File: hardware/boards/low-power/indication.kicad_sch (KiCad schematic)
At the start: 14 parts, among them Q1 DMN2400UFB4, U5 IS31FL3197

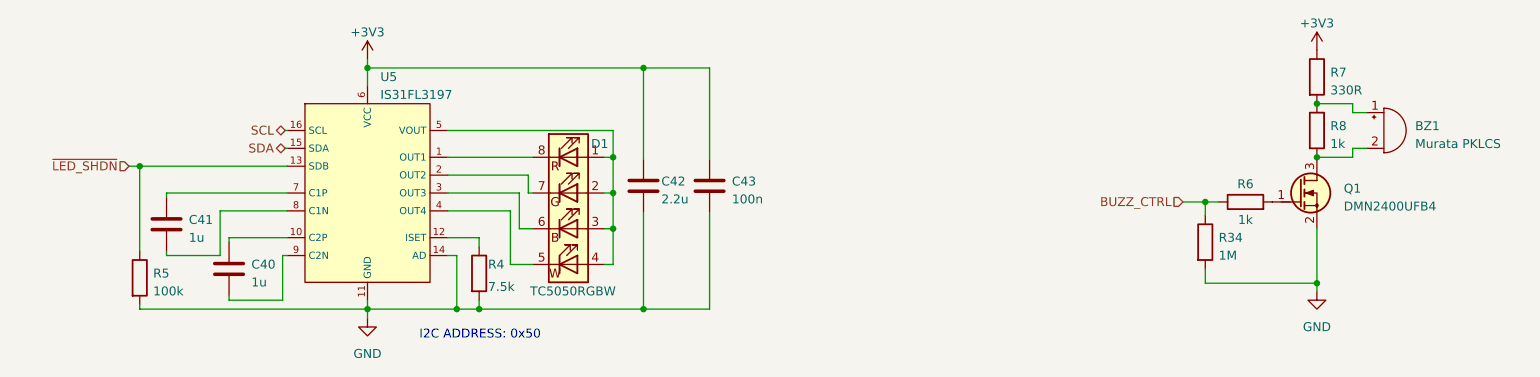
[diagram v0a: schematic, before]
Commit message: Add footprints and models for LP board
Also completed rough layout for LP board to estimate board space usage.
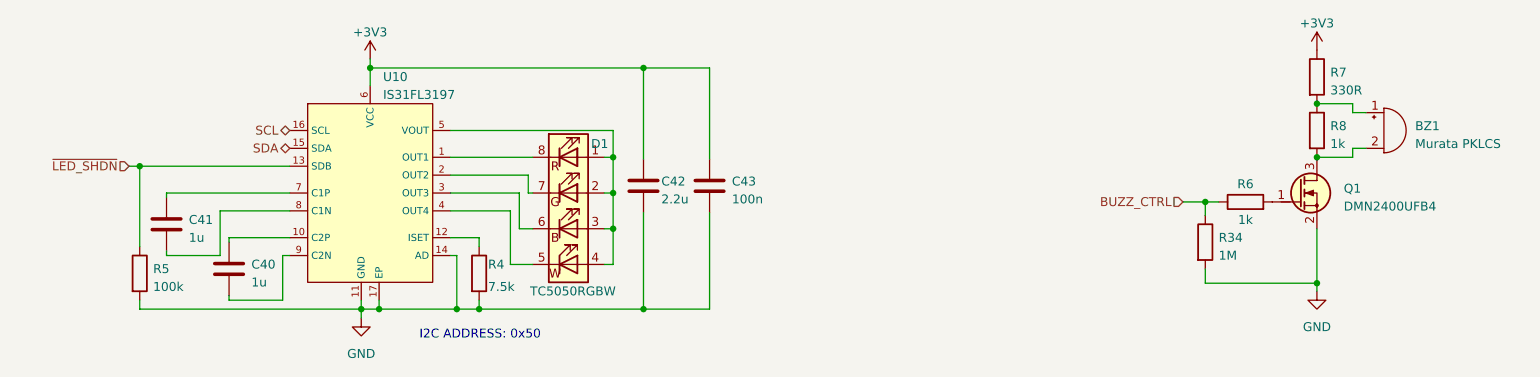
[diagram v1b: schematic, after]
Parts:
- removed U5: IS31FL3197, Package_DFN_QFN:QFN-16-1EP_4x4mm_P0.65mm_EP2.1x2.1mm, symbol Capstone:IS31FL3197
- added U10: IS31FL3197, Package_DFN_QFN:QFN-16-1EP_4x4mm_P0.65mm_EP2.1x2.1mm, symbol Capstone:IS31FL3197
- BZ1: footprint Buzzer_Beeper:Buzzer_Murata_PKLCS1212E -> capstone:Buzzer_Murata_PKLCS1212E
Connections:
- net +3V3: now also U10.6 (VCC)
- net GND: now also U10.11 (GND), U10.14 (AD), U10.17 (EP)
- net SCL: now also U10.16 (SCL)
- net SDA: now also U10.15 (SDA)
- net ~{LED_SHDN}: now also U10.13 (SDB)
- net at C40.1: now also U10.10 (C2P)
- net at C40.2: now also U10.9 (C2N)
- net at D1.1 (RA), D1.2 (GA), D1.3 (BA)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: now also U10.5 (VOUT)
- net at D1.5 (BK): now also U10.4 (OUT4)
- net at D1.6 (BK): now also U10.3 (OUT3)
- net at D1.7 (GK): now also U10.2 (OUT2)
- net at D1.8 (RK): now also U10.1 (OUT1)
- net at C41.1: now also U10.7 (C1P)
- net at C41.2: now also U10.8 (C1N)
- net at R4.1: now also U10.12 (ISET)
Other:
- moved on the sheet: R5

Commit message: Add initial changes after schematic review
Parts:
- added C803: 1u, symbol Device:C
- R34: value 1M -> 100k
- renumbered U10 to U801
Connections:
- net GND: now also C803.2
- net at D1.1 (RA), D1.2 (GA), D1.3 (BA)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: now also C803.1
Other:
- moved on the sheet: C42, C43
